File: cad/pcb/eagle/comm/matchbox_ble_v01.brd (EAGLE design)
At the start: 38 x 31 mm, 24 parts, among them J1 DF12-32-DS, J2 DF12-32-DS, P1 DF12-32-DP, P2 DF12-32-DP, U1 NRF8001, U5 2450BM14A0002, Y1 NX3225SA-16

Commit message: BT tweaks
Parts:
- removed TP1, TP2, TP3: TEST-POINT3X5, SparkFun-Passives:PAD.03X.05
- added R3, R4, R5: 0K, SparkFun-Passives:0805
- moved C4 9.26 mm to (9.75, 4.12), turned to 90 degrees
- moved D1 2.65 mm to (1.25, 21.4), turned to 180 degrees
- moved C2 0.66 mm to (21.6, 17.9)
- moved R1 0.38 mm to (16.3, 25.9)
- moved R2 0.25 mm to (16.4, 18.9)
- flipped U$1 to the top
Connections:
- net N$3 renamed ANT2
- net N$6 renamed ANT1
- net ACTIVE: no longer TP1.P$1
- net PA9: now also R3.1
- net PB3: now also U1.11
- net PB4: now also U1.14
- net PB5: now also U1.13
- net PB6: now also R4.1
- net PB7: now also R5.1
- net PC10: no longer U1.11
- net PC11: no longer U1.14
- net PC12: no longer U1.13
- net RDYN: now also R3.2
- net RXD: now also R4.2; no longer TP2.P$1
- net TXD: now also R5.2; no longer TP3.P$1
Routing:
- net PC12: track 49.8 -> 2.85 mm, vias 6 -> 1
- net RDYN: track 0.00 -> 41.8 mm, vias 0 -> 6
- net PB4: track 2.65 -> 36.7 mm, vias 1 -> 3
- net RXD: track 0.00 -> 30.8 mm, vias 0 -> 4
- net PB3: track 2.85 -> 28.0 mm, vias 1 -> 2
- net VCC_3V3: track 60.1 -> 85.1 mm
- net PB5: track 2.85 -> 27.4 mm, vias 1 -> 3
- net PC11: track 51.9 -> 27.5 mm, vias 6 -> 5
- net PC10: track 48.8 -> 24.8 mm, vias 4 -> 2
- net TXD: track 0.00 -> 23.1 mm, vias 0 -> 2
- net PC9: track 26.0 -> 36.7 mm, vias 1 -> 2
- net PC8: track 33.8 -> 24.4 mm, vias 2 -> 3
- net GND: track 24.0 -> 15.8 mm, vias 5 -> 42
- net PB6: track 2.85 -> 10.2 mm, vias 1 -> 2
- net ACTIVE: track 12.6 -> 8.44 mm, vias 2 -> 0
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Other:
- board text added: "Jimduino nRF8001"
- board text added: "RXD"
- board text added: "TXD"
- board text removed: "Jimduino RF Board"

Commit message: More progress on v01 BLE
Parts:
- moved ANT1 1.00 mm to (31.8, 29.4)
- moved C1 1.00 mm to (26.8, 19.9)
- moved C10 1.00 mm to (26.8, 18.8)
- moved C2 1.00 mm to (22.6, 17.9)
- moved C3 1.00 mm to (20.3, 17.9)
- moved C4 1.00 mm to (10.8, 4.12)
- moved C5 1.00 mm to (24.1, 26.7)
- moved C6 1.00 mm to (17.3, 24.4)
- moved C7 1.00 mm to (17.3, 20.4)
- moved C9 1.00 mm to (20.4, 25.5)
- moved D1 1.00 mm to (2.25, 21.4)
- moved J1 1.00 mm to (6.00, 15.0)
- moved J2 1.00 mm to (34.0, 15.0)
- moved P1 1.00 mm to (6.00, 15.0)
- moved P2 1.00 mm to (34.0, 15.0)
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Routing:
- net PC12: track 2.85 -> 21.0 mm, vias 1 -> 2
- net PB5: track 27.4 -> 36.3 mm
- net RXD: track 30.8 -> 32.8 mm, vias 4 -> 5
- net RESET#: track 50.3 -> 52.1 mm, vias 6 -> 9
- net PA14: track 2.75 -> 4.50 mm
- net TXD: track 23.1 -> 22.0 mm, vias 2 -> 3
- net PC11: track 27.5 -> 28.5 mm
- net PB3: track 28.0 -> 28.8 mm
- net PB4: track 36.7 -> 37.6 mm
- net PD2: track 21.6 -> 21.2 mm, vias 3 -> 2
- net PB6: track 10.2 -> 10.1 mm, vias 2 -> 1
- net GND: vias 42 -> 43
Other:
- board size 38 x 31 mm -> 40 x 32 mm

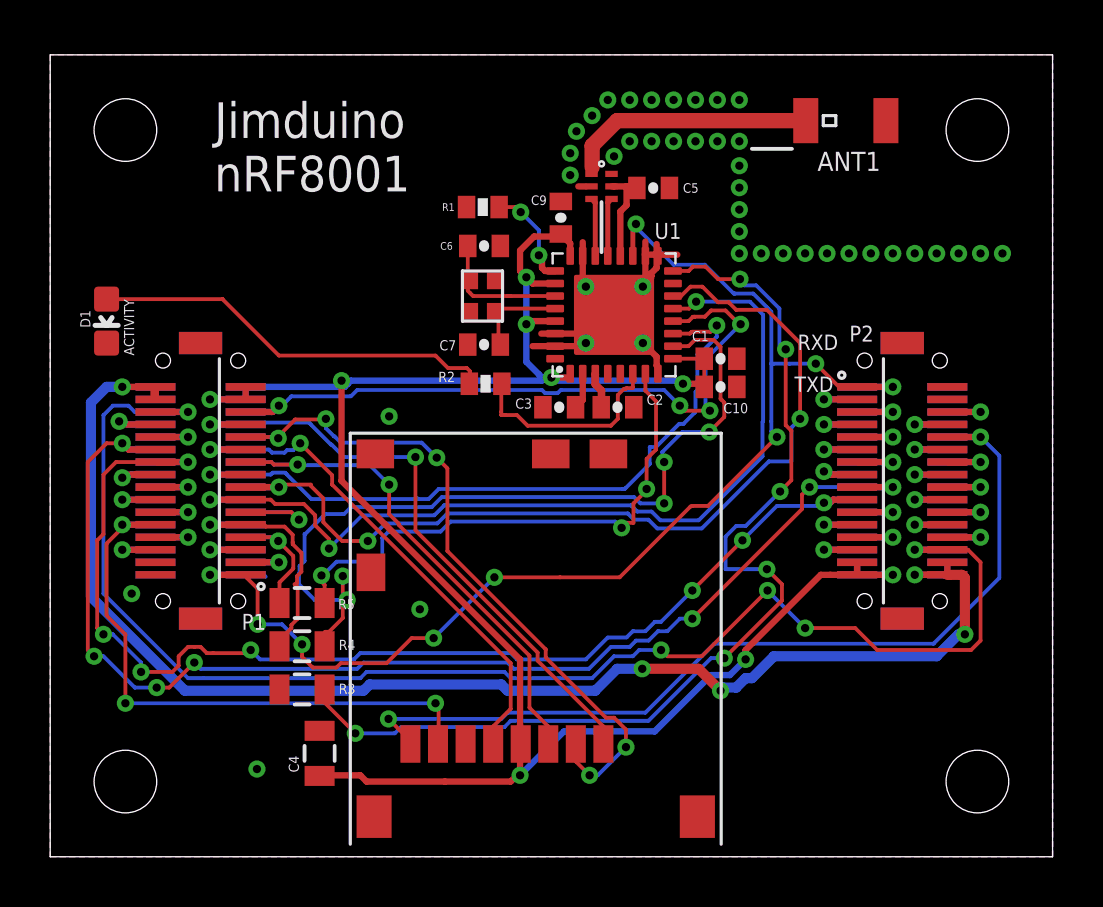
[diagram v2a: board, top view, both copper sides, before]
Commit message: Switch BLE to 40x32mm form factor
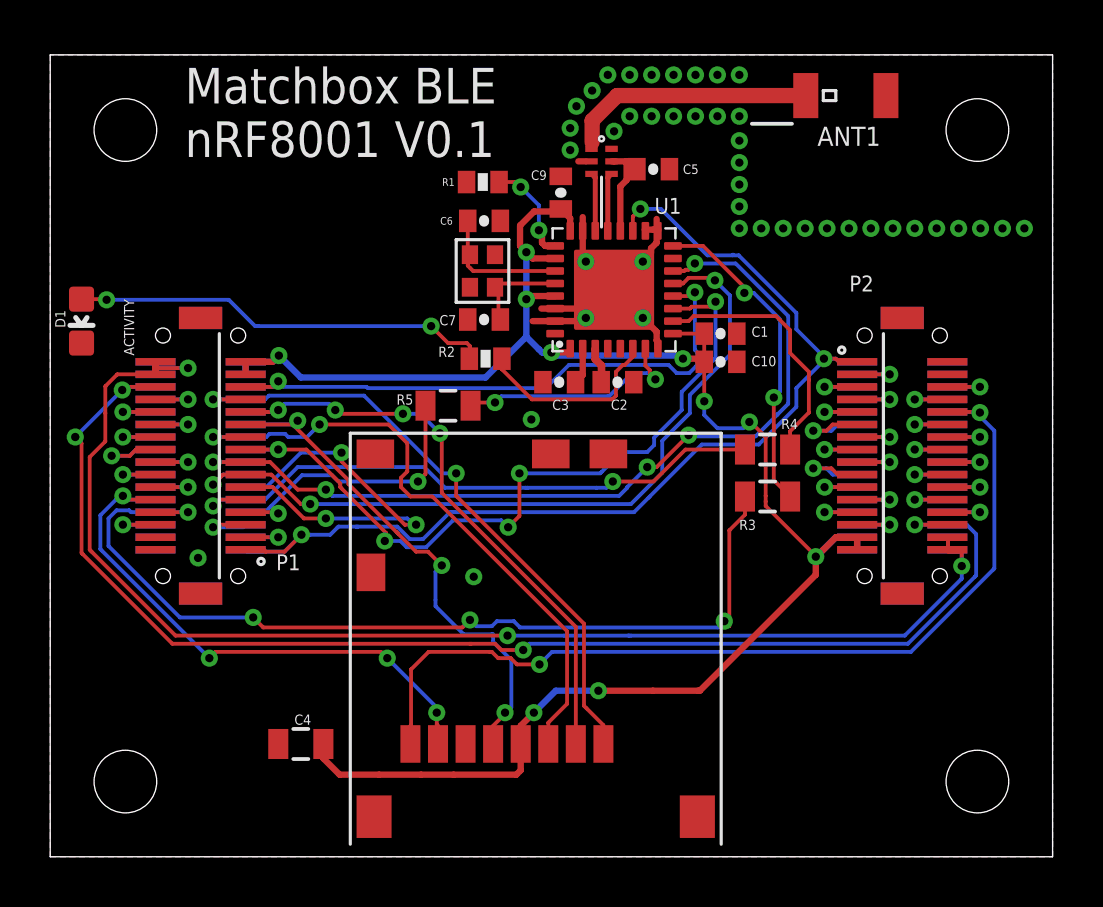
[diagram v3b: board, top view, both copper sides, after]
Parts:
- Y1: value NX3225SA-16 -> 8Y-16.000MAAV-T; device tinycircuits:ABM11 -> micro1292:ABM11
- moved R4 20.2 mm to (28.6, 16.2)
- moved R3 20.1 mm to (28.6, 14.4)
- moved R5 9.80 mm to (15.9, 18.0)
- moved ANT1 1.00 mm to (31.8, 30.4)
- moved C1 1.00 mm to (26.8, 20.9)
- moved C10 1.00 mm to (26.8, 19.8)
- moved C2 1.00 mm to (22.6, 18.9)
- moved C3 1.00 mm to (20.3, 18.9)
- moved C6 1.00 mm to (17.3, 25.4)
- moved C7 1.00 mm to (17.3, 21.4)
- moved C9 1.00 mm to (20.4, 26.5)
- moved D1 1.00 mm to (1.25, 21.4)
- moved J1 1.00 mm to (6.00, 16.0)
- moved J2 1.00 mm to (34.0, 16.0)
- moved P1 1.00 mm to (6.00, 16.0)
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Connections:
- new net RSV2: J2.17, P2.17
- new net RSV3: J2.19, P2.19
- net PC4: no longer J2.19, P2.19
- net PC5: no longer J2.17, P2.17
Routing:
- net PC5: track 50.4 -> 2.60 mm, vias 7 -> 1
- net PC4: track 47.5 -> 2.60 mm, vias 7 -> 1
- net PA9: track 2.60 -> 37.9 mm, vias 1 -> 4
- net RDYN: track 41.8 -> 13.1 mm, vias 6 -> 2
- net RXD: track 32.8 -> 10.4 mm, vias 5 -> 0
- net PB6: track 10.1 -> 24.2 mm, vias 1 -> 2
- net TXD: track 22.0 -> 9.58 mm, vias 3 -> 2
- net PA14: track 4.50 -> 16.2 mm, vias 1 -> 3
- net RESET#: track 52.1 -> 43.8 mm, vias 9 -> 3
- net VCC_3V3: track 85.1 -> 77.7 mm, vias 9 -> 10
- net PB7: track 5.68 -> 12.5 mm, vias 1 -> 2
- net VCC: track 60.1 -> 54.8 mm, vias 5 -> 3
- net PB5: track 36.3 -> 31.5 mm
- net PD2: track 21.2 -> 25.5 mm
- net GND: track 15.8 -> 11.6 mm
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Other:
- board text added: "Matchbox BLE nRF8001 V0.1"
- board text removed: "Jimduino nRF8001"
- board text removed: "RXD"
- board text removed: "TXD"

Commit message: Add VDDA supply (WIP)
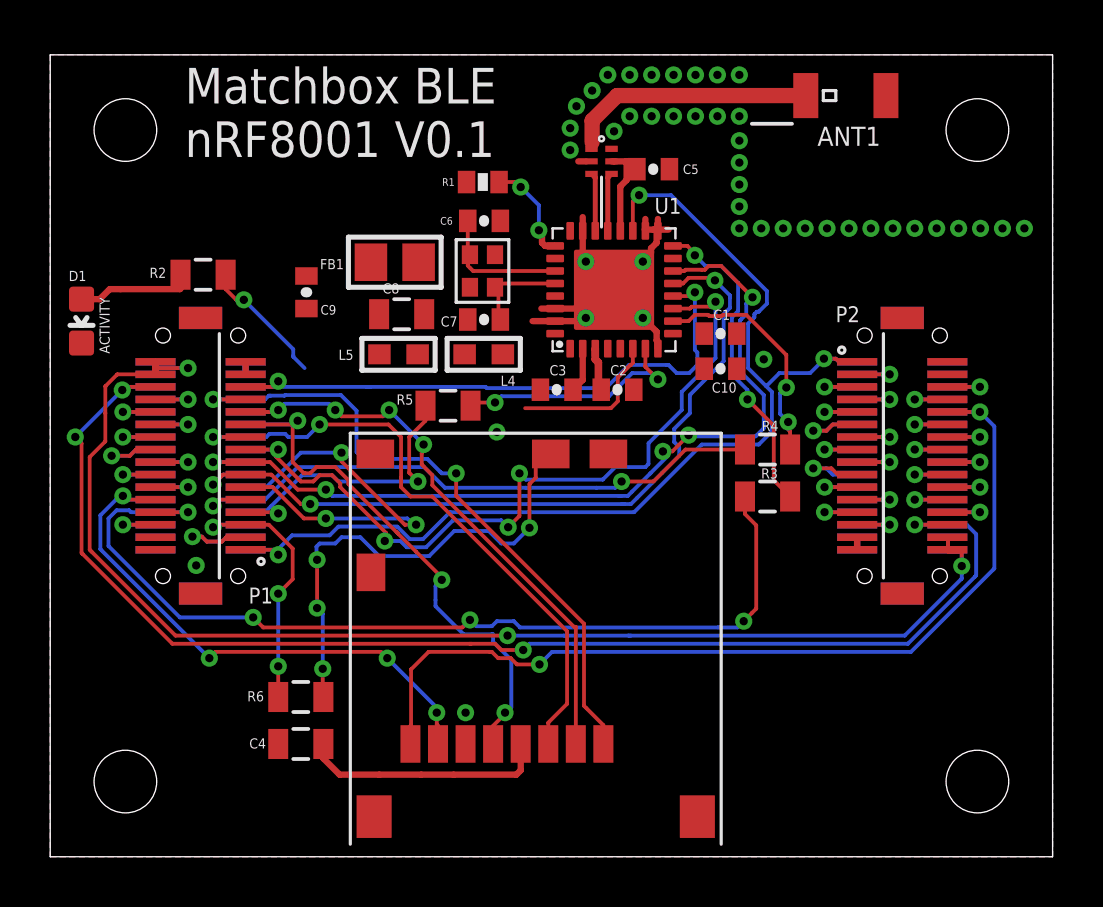
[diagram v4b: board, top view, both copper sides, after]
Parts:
- added C8: 0.1µF, SparkFun-Capacitors:0805
- added FB1: MMZ1608B121C, microbuilder:0805
- added L4: 10µH, microbuilder:_0603
- added L5: 15nH, microbuilder:_0603
- added R6: 0K, SparkFun-Passives:0805
- R2: value 22K -> 1K; device SparkFun-Passives:0402-RES -> SparkFun-Passives:0805
- moved R2 11.8 mm to (6.10, 23.2)
- moved C9 10.9 mm to (10.2, 22.5), turned to 270 degrees
- moved C3 0.32 mm to (20.2, 18.6)
- moved C2 0.30 mm to (22.6, 18.6)
- moved C10 0.27 mm to (26.8, 19.5)
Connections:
- new net AVDD: C8.1, FB1.2, L5.2, U1.24, U1.26, U1.29
- new net DCC: L4.1, U1.32
- new net DET: R6.2, U$1.DET
- new net N$3: L4.2, L5.1
- net GND: now also C8.2
- net PB8: now also R6.1
- net VCC_3V3: now also FB1.1; no longer U1.24, U1.26, U1.29
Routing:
- net VCC_3V3: track 77.7 -> 12.4 mm, vias 10 -> 0
- net DET: track 0.00 -> 19.6 mm, vias 0 -> 4
- net N$10: track 16.8 -> 4.68 mm, vias 2 -> 0
- net PB8: track 2.68 -> 11.1 mm, vias 1 -> 3
- net ACTIVE: track 7.73 -> 11.7 mm, vias 0 -> 1
- net PB9: track 2.60 -> 4.56 mm
- net RESET#: track 43.8 -> 45.2 mm
- net PC12: track 22.1 -> 23.2 mm
- net PB3: track 31.2 -> 32.2 mm
- net PC10: track 25.6 -> 26.6 mm
- net RXD: track 10.4 -> 9.39 mm, vias 0 -> 2
- net GND: track 11.6 -> 12.4 mm, vias 43 -> 44

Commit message: Final BLE board
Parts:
- removed C8: 0.1µF, SparkFun-Capacitors:0805
- removed FB1: MMZ1608B121C, microbuilder:0805
- removed L4: 10µH, microbuilder:_0603
- removed L5: 15nH, microbuilder:_0603
- C1, C3: value 0.1uF -> 100nF
- C10: value 1uF -> 100nF
- C9: value 2.2nF -> 1nF
- moved C9 10.9 mm to (20.4, 26.5), turned to 90 degrees
- moved C1 8.37 mm to (18.4, 20.0), turned to 180 degrees
- moved C10 1.32 mm to (26.8, 20.8)
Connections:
- net RDYN renamed RDY#
- removed net AVDD: C8.1, FB1.2, L5.2, U1.24, U1.26, U1.29
- removed net DCC: L4.1, U1.32
- removed net N$3: L4.2, L5.1
- net GND: no longer C8.2
- net VCC_3V3: now also U1.24, U1.26, U1.29; no longer FB1.1
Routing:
- net VCC_3V3: track 12.4 -> 81.2 mm, vias 0 -> 10
- net ACTIVE: track 11.7 -> 22.0 mm, vias 1 -> 2
- net GND: track 12.4 -> 13.3 mm
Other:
- board text added: "DET"
- board text added: "RDY#"
- board text added: "RXD"
- board text added: "TXD"
